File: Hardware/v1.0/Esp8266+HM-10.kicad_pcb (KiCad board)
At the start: 2 copper layers, 27 parts, among them P1 USB_A, P2 CONN_02X04, SW1 USER_SW, SW2 RST_SW, SW3 Mode, U1 AMS1117-3V3, U2 ESP-12E, U3 HM-10

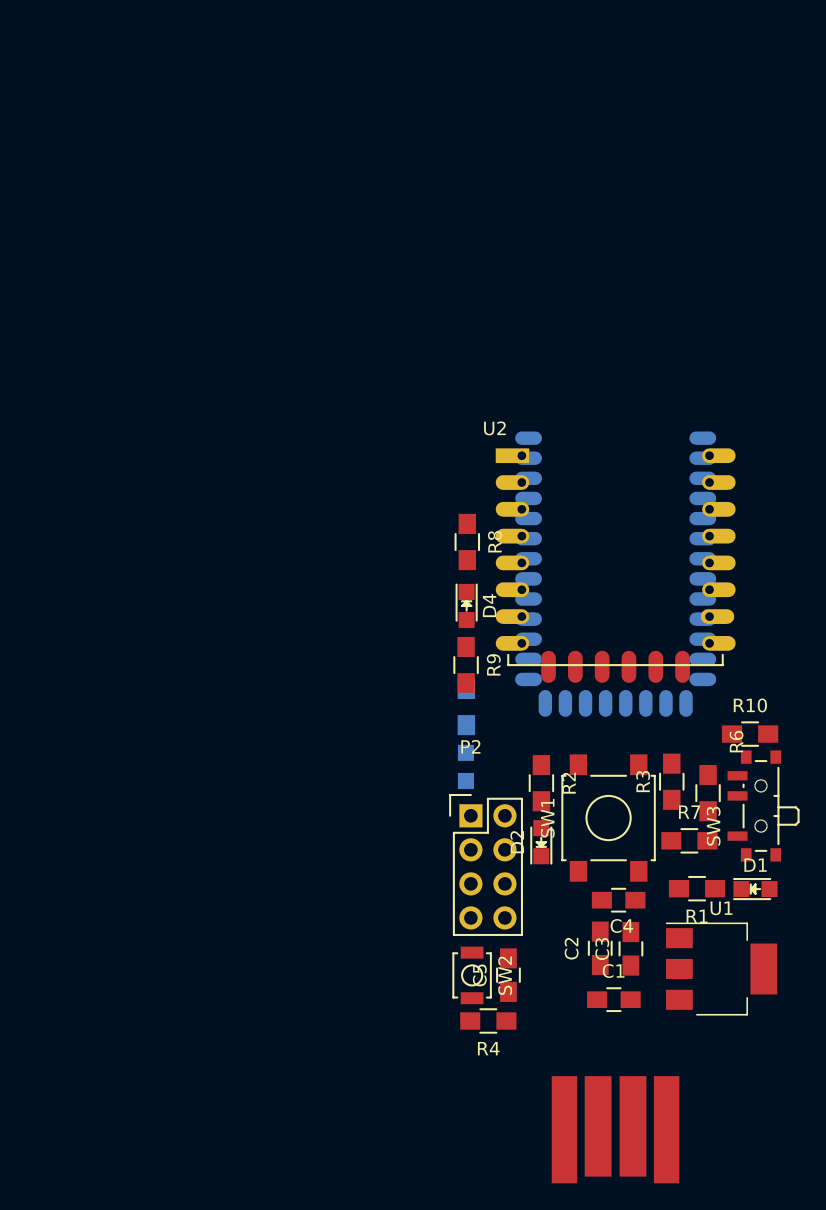
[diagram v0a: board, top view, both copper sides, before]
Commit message: Schematic and layout changed
- Schematic
i removed 2x4 header and added 1x5 ,1x4 header
- layout changed
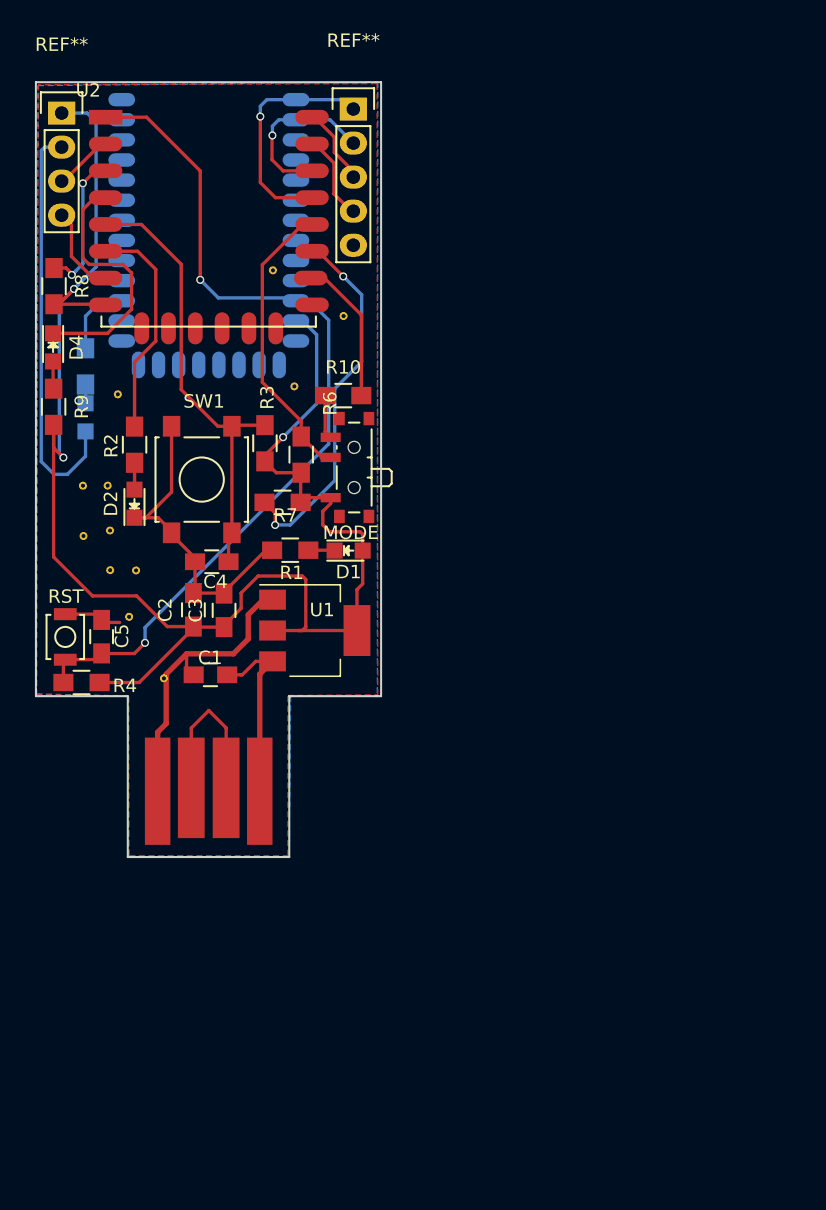
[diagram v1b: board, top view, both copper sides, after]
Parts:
- removed P2: CONN_02X04, Pin_Headers:Pin_Header_Straight_2x04
- added G***: LOGO, logos:thingTronics_10mm, B.Cu at (130.1, 101.9)
- added REF**: VIA_0.6mm, VIA'S:VIA_0.6mm, F.Cu at (134.3, 78.2)
- added REF**: VIA_0.6mm, VIA'S:VIA_0.6mm, F.Cu at (123.6, 104.0)
- added REF**: VIA_0.6mm, VIA'S:VIA_0.6mm, F.Cu at (126.2, 108.6)
- added REF**: Pin_Header_Straight_1x04, Pin_Headers:Pin_Header_Straight_1x04, F.Cu at (118.6, 66.5)
- added REF**: Pin_Header_Straight_1x04, Pin_Headers:Pin_Header_Straight_1x05, F.Cu at (140.3, 66.2)
- added REF**: VIA_0.6mm, VIA'S:VIA_0.6mm, F.Cu at (124.1, 100.6)
- added REF**: VIA_0.6mm, VIA'S:VIA_0.6mm, F.Cu at (122.8, 87.4)
- added REF**: VIA_0.6mm, VIA'S:VIA_0.6mm, F.Cu at (122.2, 97.6)
- added REF**: VIA_0.6mm, VIA'S:VIA_0.6mm, F.Cu at (122.0, 94.2)
- added REF**: VIA_0.6mm, VIA'S:VIA_0.6mm, F.Cu at (120.2, 94.2)
- added REF**: VIA_0.6mm, VIA'S:VIA_0.6mm, F.Cu at (120.2, 98.0)
- added REF**: VIA_0.6mm, VIA'S:VIA_0.6mm, F.Cu at (122.2, 100.5)
- added REF**: VIA_0.6mm, VIA'S:VIA_0.6mm, F.Cu at (135.9, 86.8)
- added REF**: VIA_0.6mm, VIA'S:VIA_0.6mm, F.Cu at (139.6, 81.6)
- moved D1 39.5 mm to (140.0, 99.1)
- moved C2 39.5 mm to (128.4, 103.5)
- moved R2 39.5 mm to (124.0, 91.2)
- moved R4 39.5 mm to (120.0, 108.9)
- moved U1 39.5 mm to (137.4, 105.1)
- moved U2 39.5 mm to (122.5, 66.8)
- moved C3 39.5 mm to (130.7, 103.5)
- moved C4 39.5 mm to (129.8, 99.9)
- moved D2 39.5 mm to (124.0, 95.6)
- moved MODE 39.5 mm to (140.1, 92.9)
- moved P1 39.5 mm to (129.5, 121.9)
- moved R1 39.5 mm to (135.6, 99.1)
- moved R10 39.5 mm to (139.6, 87.5)
- moved R3 39.5 mm to (133.7, 91.1)
- moved R6 39.5 mm to (136.4, 91.9)
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- renumbered SW3 to MODE, SW2 to RST
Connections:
- U2 pad 13: HM_TX -> HM_RX
- U2 pad 14: HM_RX -> HM_TX
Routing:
- net +3V3: track 0.00 -> 125.2 mm, vias 0 -> 3
- net GND: track 0.00 -> 87.0 mm
- net HM_RESET: track 0.00 -> 64.7 mm, vias 0 -> 2
- net GPIO14: track 0.00 -> 33.1 mm
- net GPIO2: track 0.00 -> 28.3 mm, vias 0 -> 2
- net GPIO0: track 0.00 -> 21.1 mm
- net GPIO16: track 0.00 -> 19.8 mm
- net HM_RX: track 0.00 -> 16.8 mm, vias 0 -> 1
- net GPIO12: track 0.00 -> 16.0 mm
- net +5V: track 0.00 -> 13.9 mm
- net Net-(P1-Pad2): track 0.00 -> 12.6 mm
- net HM_TX: track 0.00 -> 12.1 mm, vias 0 -> 1
- net CH_PD: track 0.00 -> 11.6 mm, vias 0 -> 2
- net GPIO15: track 0.00 -> 11.5 mm
- net GPIO13: track 0.00 -> 7.29 mm
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- added copper zone on B.Cu, net GND
- added copper zone on F.Cu, net GND
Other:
- board outline added: 25.8 x 57.8 mm
- net class Others added: clearance 0.2, trace_width 0.25, via_dia 0.6, via_drill 0.4
- net class VCC added: clearance 0.3, trace_width 0.6, via_dia 0.8, via_drill 0.4
- board text added: "3V3"
- board text added: "ADC"
- board text added: "BOOT"
- board text added: "ESP_RX"
- board text added: "ESP_TX"
- board text added: "GND"
- board text added: "GPIO13"
- board text added: "HM_RX"
- board text added: "HM_TX"
- board text added: "UART"
- board text added: "WiTooth v1.0"
